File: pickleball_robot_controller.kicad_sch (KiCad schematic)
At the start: 111 parts, among them J1 BATTERY_XT60_PIGTAIL, J10 PI_UART_CONTROL, J11 SERVO_6V_POWER_OUT, J12 MAIN_SWING_25KG_SERVO, J13 ELBOW_MG996R_SERVO, J14 WRIST_MG90S_SERVO, J2 ESP32_PICO_KIT_V4.1_CARRIER, J4 LEFT_GA25_370_MOTOR_ENCODER, J5 RIGHT_GA25_370_MOTOR_ENCODER, J9 PI POWER: 2x5V + 2xGND, U1 LM2596S-5.0, U10 TPS54560BDDA — 6V / 5A, U2 VNH5019A-E, U3 VNH5019A-E, U4 TPS54560BDDA — 5V / 5A, U5 PCA9685PW, U6 74LVC1G14, U7 74LVC1G14, U8 74LVC1G14, U9 74LVC1G14

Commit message: Rebuild controller as readable KiCad hierarchy
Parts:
- removed C1: 1000uF 25V LOW_ESR, Capacitor_THT:CP_Radial_D10.0mm_P5.00mm, symbol Device:C_Polarized
- removed C12, C15: 470uF 25V LOW_ESR, Capacitor_THT:CP_Radial_D8.0mm_P3.50mm, symbol Device:C_Polarized
- removed C2: 1uF 25V X7R, Capacitor_SMD:C_0805_2012Metric, symbol Device:C
- removed C30: 1000uF 10V LOW ESR, Capacitor_THT:CP_Radial_D10.0mm_P5.00mm, symbol Device:C_Polarized
- removed C31, C45: 100nF BOOT, Capacitor_SMD:C_0805_2012Metric, symbol Device:C
- removed C32, C33, C34, C35, C46, C47: 2.2uF 25V X7R, Capacitor_SMD:C_0805_2012Metric, symbol Device:C
- removed C36, C48: 4.7nF COMP, Capacitor_SMD:C_0805_2012Metric, symbol Device:C
- removed C37, C49: 47pF COMP, Capacitor_SMD:C_0805_2012Metric, symbol Device:C
- removed C38, C39, C50: 220uF 10V LOW ESR, Capacitor_THT:CP_Radial_D8.0mm_P3.50mm, symbol Device:C_Polarized
- removed C4: 100nF ADC FILTER, Capacitor_SMD:C_0805_2012Metric, symbol Device:C
- removed C40: 2200uF 10V LOW_ESR, Capacitor_THT:CP_Radial_D12.5mm_P5.00mm, symbol Device:C_Polarized
- removed C41, C42: 100nF, Capacitor_SMD:C_0805_2012Metric, symbol Device:C
- removed C43: 10uF 10V X7R, Capacitor_SMD:C_0805_2012Metric, symbol Device:C
- removed C44, C51: 1uF 10V X7R, Capacitor_SMD:C_0805_2012Metric, symbol Device:C
- removed C5: 220uF 25V LOW_ESR, Capacitor_THT:CP_Radial_D8.0mm_P3.50mm, symbol Device:C_Polarized
- removed C7: 330uF 10V LOW_ESR, Capacitor_THT:CP_Radial_D8.0mm_P3.50mm, symbol Device:C_Polarized
- removed C76, C77, C78, C79: 1nF FILTER, Capacitor_SMD:C_0805_2012Metric, symbol Device:C
- removed C80, C90: 10nF CURRENT FILTER, Capacitor_SMD:C_0805_2012Metric, symbol Device:C
- removed D1: SMBJ18A, Diode_SMD:D_SMB, symbol Device:D_TVS
- removed D10, D9: B560C 5A, Diode_SMD:D_SMC, symbol Device:D_Schottky
- removed D3: SS54, Diode_SMD:D_SMA, symbol Device:D_Schottky
- removed D4: SMBJ8.0A, Diode_SMD:D_SMB, symbol Device:D_TVS
- removed D5: GREEN, LED_SMD:LED_0805_2012Metric, symbol Device:LED
- removed D6: BLUE, LED_SMD:LED_0805_2012Metric, symbol Device:LED
- removed D7: AMBER, LED_SMD:LED_0805_2012Metric, symbol Device:LED
- removed D8: RED, LED_SMD:LED_0805_2012Metric, symbol Device:LED
- removed F1: 15A_EXTERNAL_BLADE, Fuse:Fuse_Blade_ATO_directSolder, symbol Device:Fuse
- removed F2: 7.5A_SERVO_OUTPUT_FUSE, Fuse:Fuse_Blade_ATO_directSolder, symbol Device:Fuse
- removed F3: 5A PI OUTPUT FUSE, Fuse:Fuse_1206_3216Metric, symbol Device:Fuse
- removed J1: BATTERY_XT60_PIGTAIL, TerminalBlock:TerminalBlock_MaiXu_MX126-5.0-02P_1x02_P5.00mm, symbol Connector_Generic:Conn_01x02
- removed J10: PI_UART_CONTROL, Connector_JST:JST_XH_B8B-XH-A_1x08_P2.50mm_Vertical, symbol Connector_Generic:Conn_01x08
- removed J11: SERVO_6V_POWER_OUT, TerminalBlock:TerminalBlock_MaiXu_MX126-5.0-02P_1x02_P5.00mm, symbol Connector_Generic:Conn_01x02
- removed J12: MAIN_SWING_25KG_SERVO, Connector_PinHeader_2.54mm:PinHeader_1x03_P2.54mm_Vertical, symbol Connector_Generic:Conn_01x03
- removed J13: ELBOW_MG996R_SERVO, Connector_PinHeader_2.54mm:PinHeader_1x03_P2.54mm_Vertical, symbol Connector_Generic:Conn_01x03
- removed J14: WRIST_MG90S_SERVO, Connector_PinHeader_2.54mm:PinHeader_1x03_P2.54mm_Vertical, symbol Connector_Generic:Conn_01x03
- removed J2: ESP32_PICO_KIT_V4.1_CARRIER, PickleballRobot:ESP32_PICO_KIT_V4_1_Carrier, symbol Connector_Generic:Conn_02x17_Odd_Even
- removed J4: LEFT_GA25_370_MOTOR_ENCODER, Connector_JST:JST_PH_B6B-PH-K_1x06_P2.00mm_Vertical, symbol Connector_Generic:Conn_01x06
- removed J5: RIGHT_GA25_370_MOTOR_ENCODER, Connector_JST:JST_PH_B6B-PH-K_1x06_P2.00mm_Vertical, symbol Connector_Generic:Conn_01x06
- removed J9: PI POWER: 2x5V + 2xGND, Connector_Molex:Molex_Mini-Fit_Jr_5569-04A2_2x02_P4.20mm_Horizontal, symbol Connector_Generic:Conn_02x02_Odd_Even
- removed L1: 33uH >=4A SHIELDED, Inductor_SMD:L_Sunlord_MWSA1265S, symbol Device:L
- removed L2, L3: XAL7070-682MEC 6.8uH, Inductor_SMD:L_Coilcraft_XAL7070-XXX, symbol Device:L
- removed R1: 100k 1% BAT DIV TOP, Resistor_SMD:R_0805_2012Metric, symbol Device:R
- removed R100, R101, R102, R103, R40, R41: 1k, Resistor_SMD:R_0805_2012Metric, symbol Device:R
- removed R104, R30: 243k RT SET, Resistor_SMD:R_0805_2012Metric, symbol Device:R
- removed R105: 590k FB TOP 1%, Resistor_SMD:R_0805_2012Metric, symbol Device:R
- removed R106, R32: 90.9k FB BOTTOM 1%, Resistor_SMD:R_0805_2012Metric, symbol Device:R
- removed R107, R33: 10.2k COMP, Resistor_SMD:R_0805_2012Metric, symbol Device:R
- removed R14, R7: 1k CURRENT SENSE, Resistor_SMD:R_0805_2012Metric, symbol Device:R
- removed R2: 27k 1% BAT DIV BOTTOM, Resistor_SMD:R_0805_2012Metric, symbol Device:R
- removed R3: 1k ADC PROTECT, Resistor_SMD:R_0805_2012Metric, symbol Device:R
- removed R31: 442k FB TOP 1%, Resistor_SMD:R_0805_2012Metric, symbol Device:R
- removed R42: 10k, Resistor_SMD:R_0805_2012Metric, symbol Device:R
- removed R50, R51: 4.7k I2C PULLUP, Resistor_SMD:R_0805_2012Metric, symbol Device:R
- removed R52: 10k OE SAFE PULLUP, Resistor_SMD:R_0805_2012Metric, symbol Device:R
- removed R60, R62, R64: 220R SIGNAL, Resistor_SMD:R_0805_2012Metric, symbol Device:R
- removed R61, R63, R65: 10k SIGNAL PULLDOWN, Resistor_SMD:R_0805_2012Metric, symbol Device:R
- removed R76, R77, R78, R79: 10k PULLUP, Resistor_SMD:R_0805_2012Metric, symbol Device:R
- removed R80, R81, R82, R90, R91, R92: 100k SAFE PULLDOWN, Resistor_SMD:R_0805_2012Metric, symbol Device:R
- removed R83, R93: 10k FAULT PULLUP, Resistor_SMD:R_0805_2012Metric, symbol Device:R
- removed U1: LM2596S-5.0, Package_TO_SOT_SMD:TO-263-5_TabPin3, symbol Regulator_Switching:LM2596S-5
- removed U10: TPS54560BDDA — 6V / 5A, Package_SO:TI_SO-PowerPAD-8_ThermalVias, symbol Regulator_Switching:TPS54560BDDA
- removed U2, U3: VNH5019A-E, Package_SO:ST_MultiPowerSO-30, symbol Driver_Motor:VNH5019A-E
- removed U4: TPS54560BDDA — 5V / 5A, Package_SO:TI_SO-PowerPAD-8_ThermalVias, symbol Regulator_Switching:TPS54560BDDA
- removed U5: PCA9685PW, Package_SO:TSSOP-28_4.4x9.7mm_P0.65mm, symbol Driver_LED:PCA9685PW
- removed U6, U7, U8, U9: 74LVC1G14, Package_TO_SOT_SMD:SOT-23-5, symbol 74xGxx:74LVC1G14
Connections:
- no-connect marks 31 -> 0
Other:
- added sheet 01 Power and Pi (01_power_and_pi.kicad_sch)
- added sheet 02 ESP32 and Pi UART (02_esp32_and_pi.kicad_sch)
- added sheet 03 Left Motor (03_left_motor.kicad_sch)
- added sheet 04 Right Motor (04_right_motor.kicad_sch)
- added sheet 05 Encoders (05_encoder_inputs.kicad_sch)
- added sheet 06 Arm Servos (06_arm_servos.kicad_sch)
- note added: "Global net labels connect the sheets. Open any sheet from the hierarchy panel."
- note added: "PICKLEBALL ROBOT CONTROLLER — SIX READABLE KICAD SHEETS"
- note removed: "1. VNH5019 exposed pads need reflow, thermal vias, and large copper pours."
- note removed: "2. Verify actual motor stall current before ordering production PCB."
- note removed: "3-DOF ARM SERVO CONTROL"
- note removed: "3. Pi power is NOT made by U1. Feed J8 from a separate regulated 5V/5A supply."
- note removed: "4. Never power ESP32 from USB and EXT_5V simultaneously."
- note removed: "5. External fuse and latching E-stop are mandatory."
- note removed: "5V CONTROL BUCK (ESP32 + LOGIC ONLY)"
- note removed: "BATTERY INPUT + PROTECTION"
- note removed: "D5 GREEN: control 5V D6 BLUE: Pi 5V D7 AMBER: servo 6V D8 RED: motor driver fault"
- note removed: "Do not connect Pi/ESP UART while Micro-USB serial is actively driving RX0/TX0."
- note removed: "ESP32-PICO-KIT V4.1 SOCKETS"
- note removed: "ESP32-PICO-KIT carrier uses the confirmed 17.78mm row spacing."
- note removed: "Encoder inputs include pull-ups, RC filtering, and Schmitt buffers."
- note removed: "External latching E-stop / disconnect goes between F1 and VBAT_SW"
- note removed: "Five amp rail is deliberate: enough for normal 3-servo operation, with the 7.5A fuse limiting the branch."
- note removed: "J4/J5 are six-pin JST-PH 2.00mm: motor+/motor-/GND/+3V3/encoder-A/encoder-B."
- note removed: "LEFT MOTOR DRIVER"
- note removed: "RASPBERRY PI 5V / 5A BUCK — TPS54560B"
- note removed: "RASPBERRY PI UART / CONTROL"
- note removed: "RIGHT MOTOR DRIVER"
- note removed: "SAFETY / REVIEW NOTES"
- note removed: "SERVO 6V / 5A BUCK — TPS54560B"
- note removed: "STATUS LEDs"
- note removed: "Servo 1 = main swing; Servo 2 = elbow; Servo 3 = wrist. Pin order: GND / regulated 6V / PWM."
- note removed: "U4 values are the TI 12V-to-5V / 5A reference design. Follow TI layout guidance; do not use this rail for motors or servos."
- note removed: "UART is 3.3V: Pi GPIO14 TX -> ESP RX0; ESP TX0 -> Pi GPIO15 RX."
- note removed: "Use Mini-Fit Jr / screw terminal, not 0.1in headers, for Pi power. Keep this 5A path short and wide."
- note removed: "WHEEL ENCODERS — BUILT INTO J4/J5 (3.3V)"
- title: Pickleball Robot Wheel Controller + Raspberry Pi Interface -> Pickleball Robot Controller — Hierarchical Overview

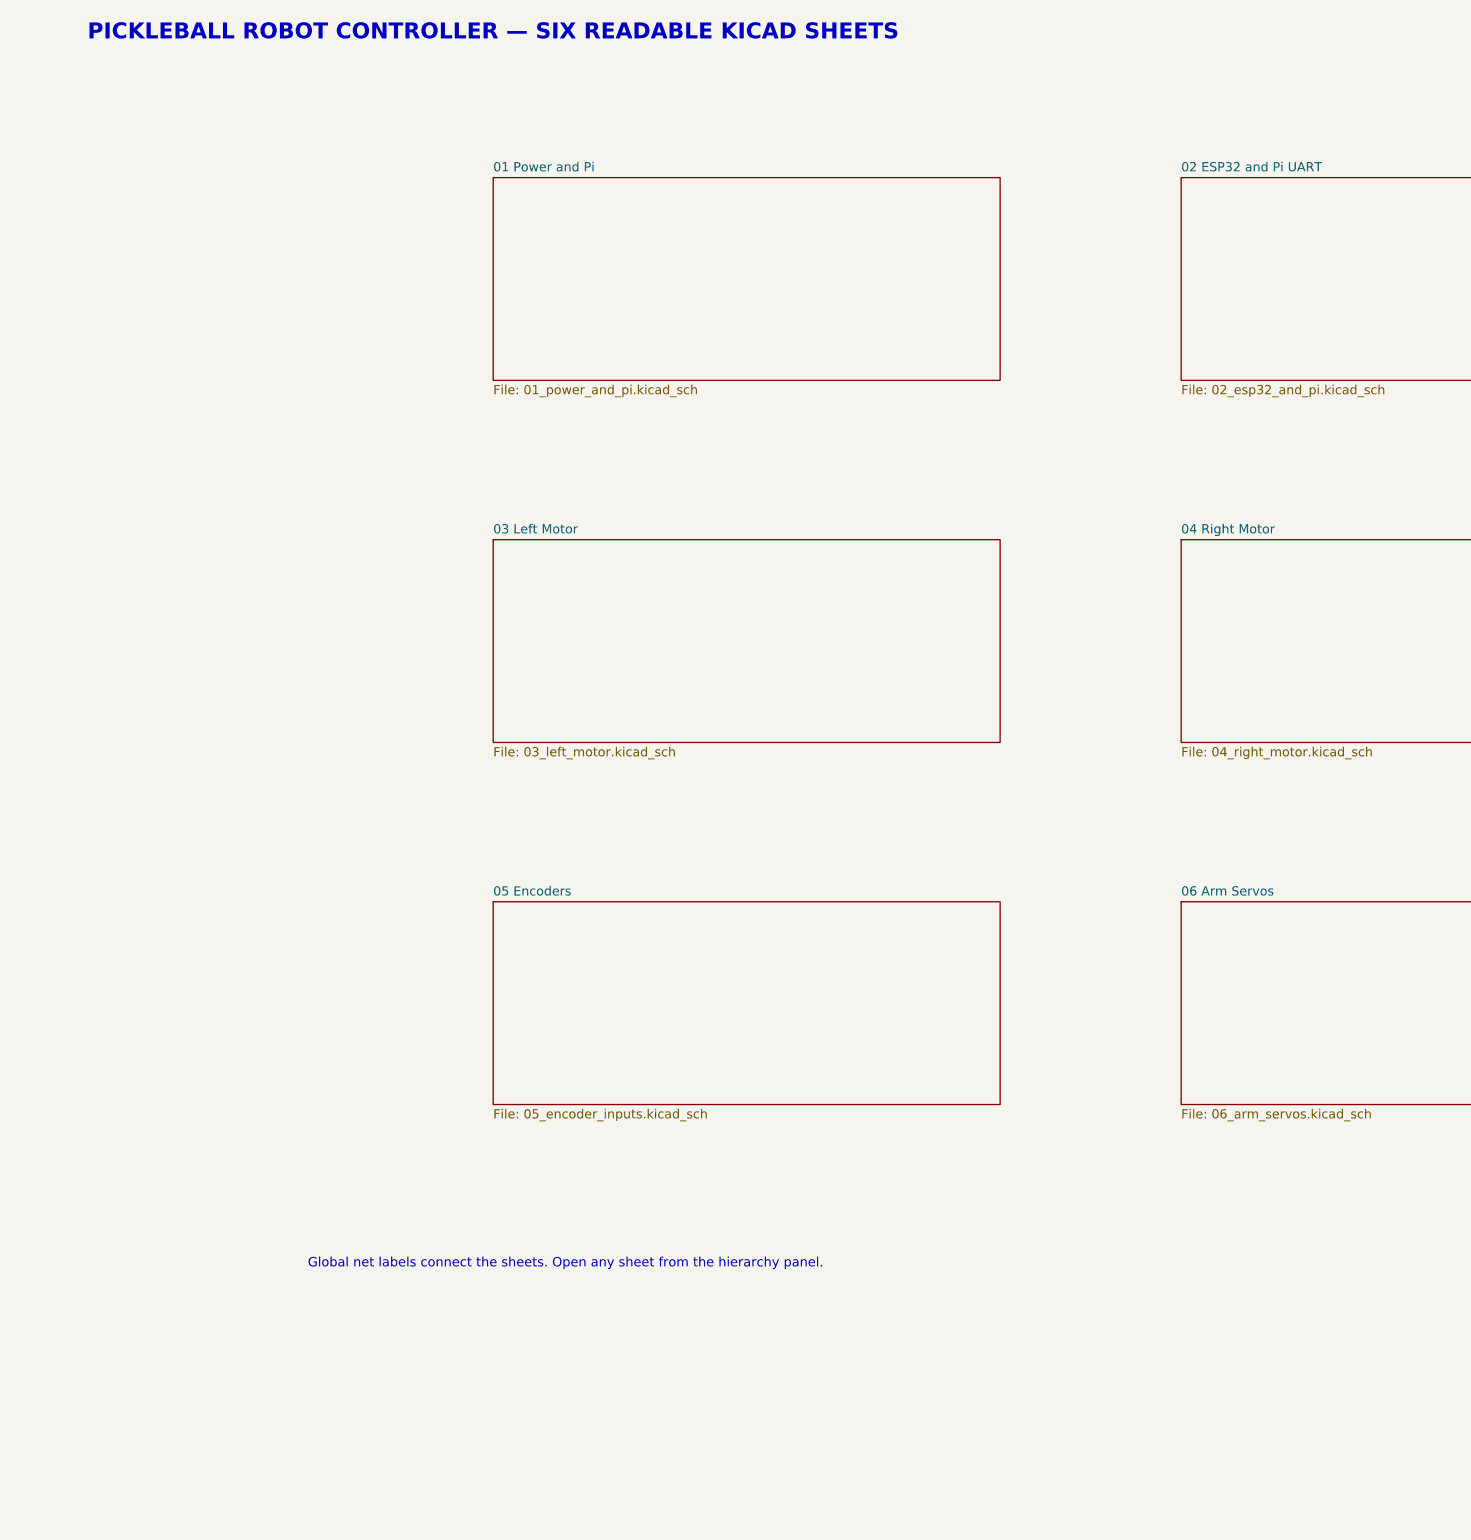
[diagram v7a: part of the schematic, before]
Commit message: Add dedicated 8.4V rail for Miuzei main servo
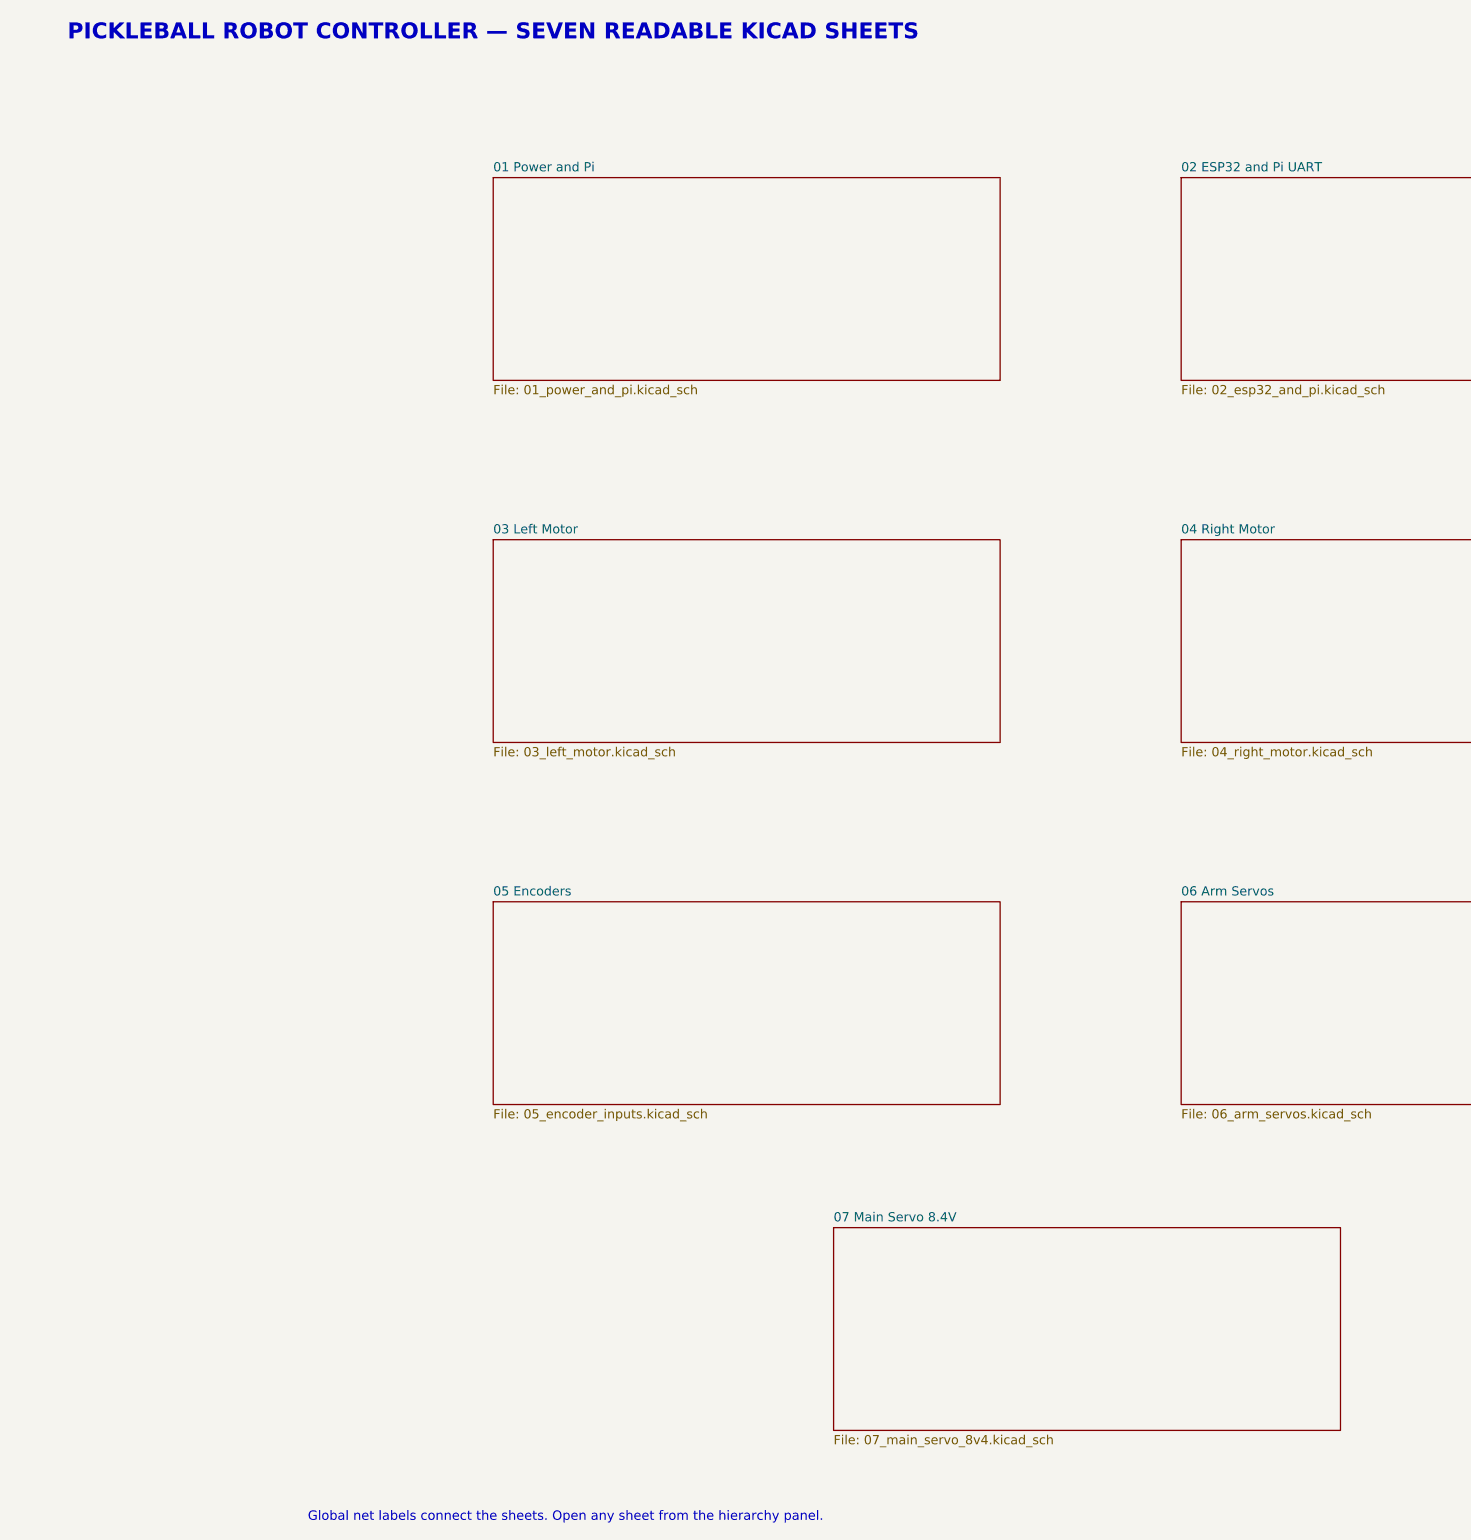
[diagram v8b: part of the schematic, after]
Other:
- added sheet 07 Main Servo 8.4V (07_main_servo_8v4.kicad_sch)
- note added: "PICKLEBALL ROBOT CONTROLLER — SEVEN READABLE KICAD SHEETS"
- note removed: "PICKLEBALL ROBOT CONTROLLER — SIX READABLE KICAD SHEETS"
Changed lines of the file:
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@@
 		(company "Harrison")
 	)
-	(text "PICKLEBALL ROBOT CONTROLLER — SIX READABLE KICAD SHEETS"
+	(text "PICKLEBALL ROBOT CONTROLLER — SEVEN READABLE KICAD SHEETS"
 		(exclude_from_sim no)
 		(at 25 20 0.0000)
@@
 	(text "Global net labels connect the sheets. Open any sheet from the hierarchy panel."
 		(exclude_from_sim no)
-		(at 35 190 0.0000)
+		(at 35 225 0.0000)
 		(effects
 			(font
@@
 		(instances
 			(project "pickleball_robot_controller"
-				(path "/008f5f25-ee15-417c-9db4-b0659030e66e"
+				(path "/6e592ef6-5e2f-4d87-a569-afbad47f123a"
 					(page "2")
 				)
@@
 		(instances
 			(project "pickleball_robot_controller"
-				(path "/008f5f25-ee15-417c-9db4-b0659030e66e"
+				(path "/6e592ef6-5e2f-4d87-a569-afbad47f123a"
 					(page "3")
 				)
@@
 		(instances
 			(project "pickleball_robot_controller"
-				(path "/008f5f25-ee15-417c-9db4-b0659030e66e"
+				(path "/6e592ef6-5e2f-4d87-a569-afbad47f123a"
 					(page "4")
 				)
@@
 		(instances
 			(project "pickleball_robot_controller"
-				(path "/008f5f25-ee15-417c-9db4-b0659030e66e"
+				(path "/6e592ef6-5e2f-4d87-a569-afbad47f123a"
 					(page "5")
 				)
@@
 		(instances
 			(project "pickleball_robot_controller"
-				(path "/008f5f25-ee15-417c-9db4-b0659030e66e"
+				(path "/6e592ef6-5e2f-4d87-a569-afbad47f123a"
 					(page "6")
 				)
@@
 		(instances
 			(project "pickleball_robot_controller"
-				(path "/008f5f25-ee15-417c-9db4-b0659030e66e"
+				(path "/6e592ef6-5e2f-4d87-a569-afbad47f123a"
 					(page "7")
 				)
 			)
+		)
+	)
+	(sheet
+		(at 72 185)
+		(size 70 28)
+		(exclude_from_sim no)
+		(in_bom yes)
+		(on_board yes)
+		(dnp no)
+		(fields_autoplaced yes)
+		(stroke
+			(width 0.1524)
+			(type solid)
+		)
+		(fill
+			(color 0 0 0 0.0000)
+		)
+		(property "Sheetname" "07 Main Servo 8.4V"
+			(at 72 184.2884 0)
+			(effects
+				(font
+					(size 1.27 1.27)
+				)
+				(justify left bottom)
+			)
+		)
+		(property "Sheetfile" "07_main_servo_8v4.kicad_sch"
+			(at 72 213.5846 0)
+			(effects
+				(font
+					(size 1.27 1.27)
+				)
+				(justify left top)
+			)
+		)
+		(instances
+			(project "pickleball_robot_controller"
+				(path "/6e592ef6-5e2f-4d87-a569-afbad47f123a"
+					(page "8")
+				)
+			)
